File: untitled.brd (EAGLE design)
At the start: 54.8 x 54.7 mm, 25 parts

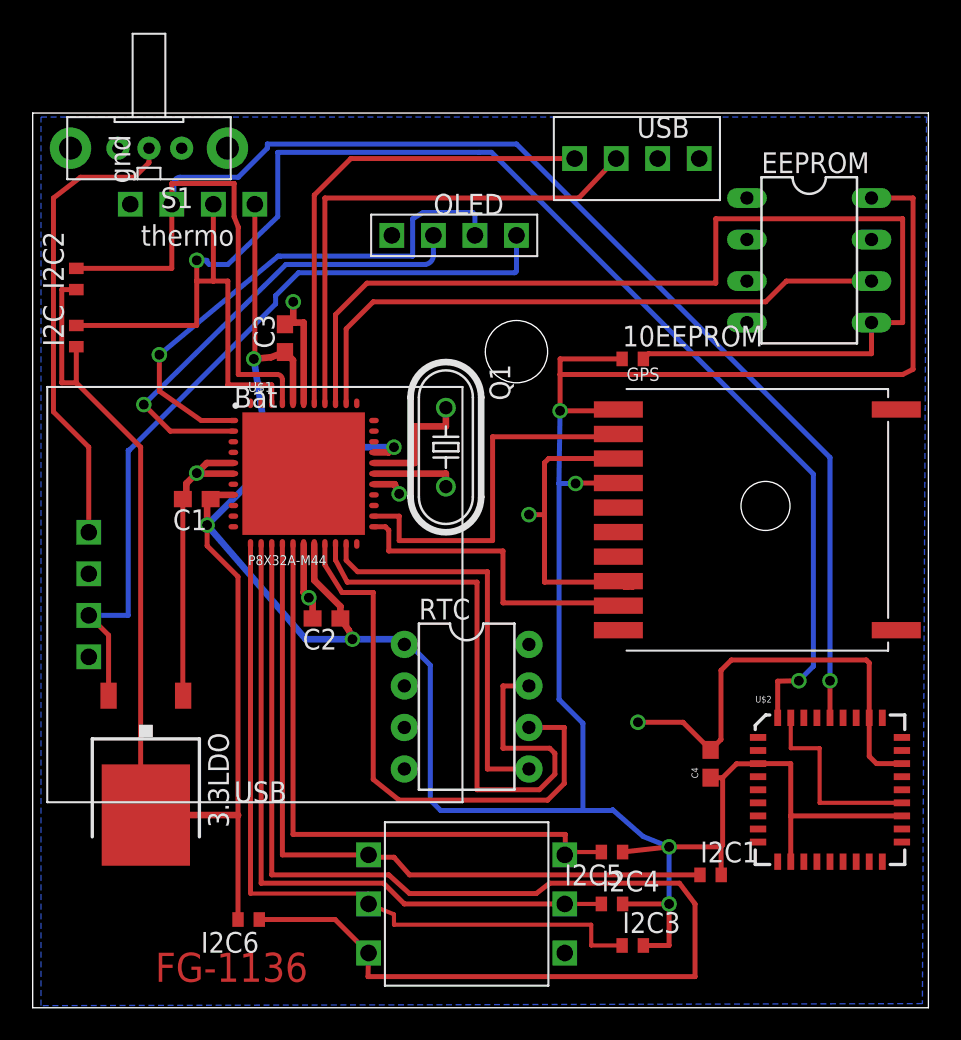
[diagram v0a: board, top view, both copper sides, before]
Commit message: fixed stupid and costly mistake with screen position
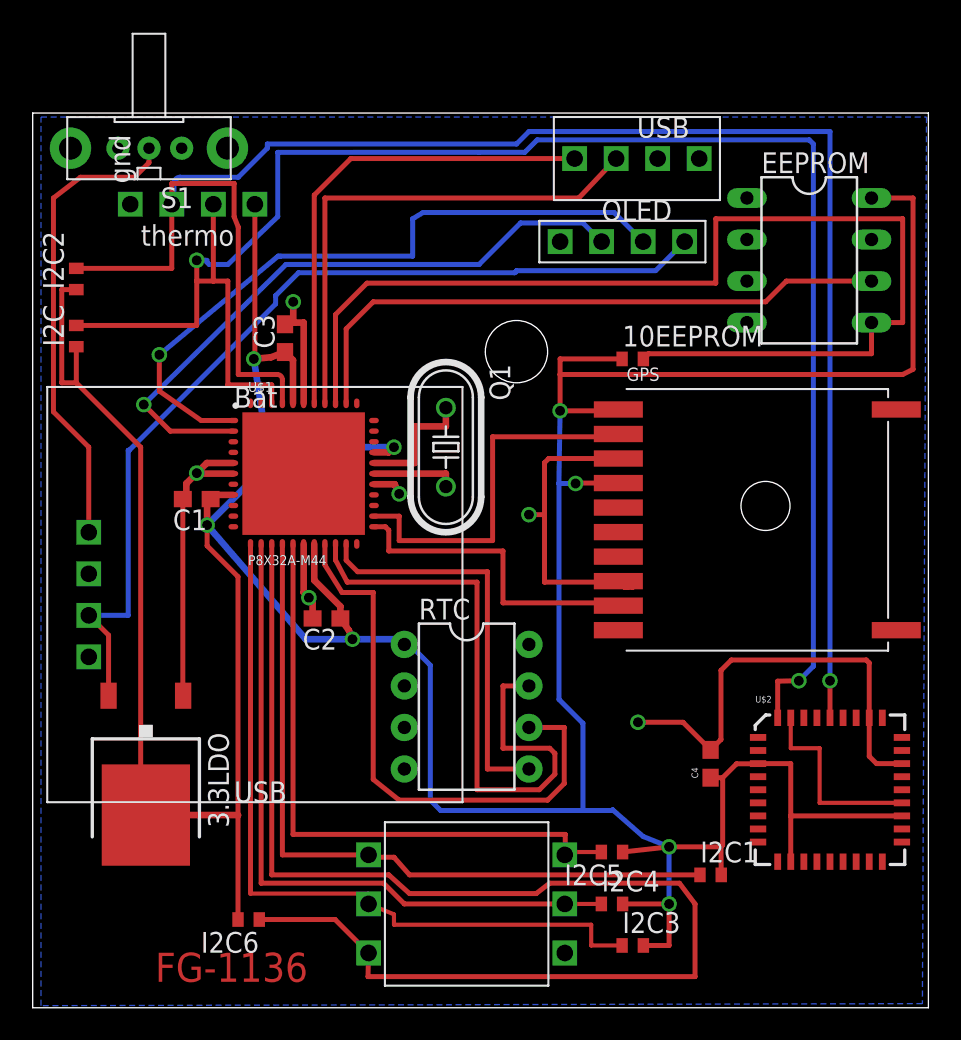
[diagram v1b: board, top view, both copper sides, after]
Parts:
- moved OLED_SCREEN 10.3 mm to (75.6, 57.0)
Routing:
- net SDA: track 95.9 -> 108.3 mm
- net SCL: track 97.3 -> 109.6 mm
- net N$10: track 28.8 -> 39.2 mm
- net N$11: track 32.5 -> 42.2 mm
- net +5V: track 48.7 -> 57.5 mm
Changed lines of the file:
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@@
 <setting verticaltext="up"/>
 </settings>
-<grid distance="0.005" unitdist="inch" unit="inch" style="lines" multiple="1" display="yes" altdistance="0.025" altunitdist="inch" altunit="inch"/>
+<grid distance="0.005" unitdist="inch" unit="inch" style="lines" multiple="1" display="no" altdistance="0.025" altunitdist="inch" altunit="inch"/>
 <layers>
 <layer number="1" name="Top" color="4" fill="1" visible="yes" active="yes"/>
@@
 <element name="GPS" library="adafruit" package="FGPMMOPA6B" value="" x="82.55" y="40.005"/>
 <element name="LIPOCHARGER-BOOSTER" library="SFLipoPack" package="SFLIPO" value="SFLIPO" x="46.736" y="36.703"/>
-<element name="OLED_SCREEN" library="4dScreen" package="4DSCREEN" value="4DSCREEN" x="65.278" y="57.404" rot="R270"/>
+<element name="OLED_SCREEN" library="4dScreen" package="4DSCREEN" value="4DSCREEN" x="75.565" y="57.023" rot="R270"/>
 <element name="RTC" library="adafruit" package="DIL08-ROUND" value="DS1302" x="64.77" y="28.575" rot="R270"/>
 <element name="S1" library="adafruit" package="EG1213" value="EG1213" x="45.339" y="62.738" rot="R180"/>
@@
 <wire x1="50.546" y1="60.579" x2="46.736" y2="60.579" width="0.3048" layer="1"/>
 <wire x1="46.736" y1="60.579" x2="46.736" y2="59.309" width="0.3048" layer="1"/>
-<wire x1="86.995" y1="43.815" x2="67.818" y2="62.992" width="0.3048" layer="16"/>
 <wire x1="67.818" y1="62.992" x2="52.578" y2="62.992" width="0.3048" layer="16"/>
 <wire x1="52.578" y1="62.992" x2="52.578" y2="62.738" width="0.3048" layer="16"/>
@@
 <wire x1="40.894" y1="55.387" x2="46.736" y2="55.387" width="0.3048" layer="1"/>
 <wire x1="46.736" y1="55.387" x2="46.736" y2="59.309" width="0.3048" layer="1"/>
-<wire x1="86.995" y1="43.815" x2="86.995" y2="30.1625" width="0.3048" layer="16"/>
 <wire x1="50.546" y1="60.579" x2="50.546" y2="58.547" width="0.3048" layer="1"/>
 <wire x1="50.546" y1="58.547" x2="50.8" y2="57.912" width="0.3048" layer="1"/>
+<wire x1="86.995" y1="30.1625" x2="86.995" y2="63.754" width="0.3048" layer="16"/>
+<wire x1="86.995" y1="63.754" x2="68.58" y2="63.754" width="0.3048" layer="16"/>
+<wire x1="68.58" y1="63.754" x2="67.818" y2="62.992" width="0.3048" layer="16"/>
 </signal>
 <signal name="SDA">
@@
 <wire x1="48.26" y1="55.88" x2="48.768" y2="55.88" width="0.3048" layer="16"/>
 <wire x1="48.768" y1="55.88" x2="48.895" y2="55.88" width="0.3048" layer="16"/>
-<wire x1="65.532" y1="62.484" x2="66.294" y2="62.484" width="0.3048" layer="16"/>
-<wire x1="66.294" y1="62.484" x2="85.979" y2="42.799" width="0.3048" layer="16"/>
 <wire x1="53.21680625" y1="62.4820625" x2="53.21680625" y2="58.55080625" width="0.3048" layer="16"/>
 <wire x1="53.21680625" y1="58.55080625" x2="50.165" y2="55.626" width="0.3048" layer="16"/>
@@
 <wire x1="48.26" y1="51.8945" x2="48.26" y2="54.61" width="0.3048" layer="1"/>
 <wire x1="85.09" y1="30.1625" x2="85.979" y2="31.0515" width="0.3048" layer="16"/>
-<wire x1="85.979" y1="31.0515" x2="85.979" y2="42.799" width="0.3048" layer="16"/>
+<wire x1="85.979" y1="31.0515" x2="85.979" y2="62.992" width="0.3048" layer="16"/>
+<wire x1="85.979" y1="62.992" x2="85.725" y2="63.246" width="0.3048" layer="16"/>
+<wire x1="85.725" y1="63.246" x2="69.088" y2="63.246" width="0.3048" layer="16"/>
+<wire x1="65.532" y1="62.484" x2="68.326" y2="62.484" width="0.3048" layer="16"/>
+<wire x1="68.326" y1="62.484" x2="69.088" y2="63.246" width="0.3048" layer="16"/>
 </signal>
 <signal name="N$3">
@@
 <wire x1="46.6437" y1="45.4313" x2="45.0215" y2="47.0535" width="0.3048" layer="1"/>
 <wire x1="45.0215" y1="47.0535" x2="53.721" y2="55.626" width="0.3048" layer="16"/>
-<wire x1="53.721" y1="55.626" x2="62.23" y2="55.626" width="0.3048" layer="16"/>
-<wire x1="62.23" y1="55.626" x2="62.738" y2="56.261" width="0.3048" layer="16" curve="90"/>
-<wire x1="62.738" y1="56.261" x2="62.738" y2="57.404" width="0.3048" layer="16"/>
+<wire x1="53.721" y1="55.626" x2="65.532" y2="55.626" width="0.3048" layer="16"/>
+<wire x1="73.025" y1="57.023" x2="71.882" y2="58.166" width="0.3048" layer="16"/>
+<wire x1="71.882" y1="58.166" x2="68.072" y2="58.166" width="0.3048" layer="16"/>
+<wire x1="68.072" y1="58.166" x2="65.532" y2="55.626" width="0.3048" layer="16"/>
 </signal>
 <signal name="N$11">
@@
 <wire x1="48.5337" y1="46.0813" x2="45.974" y2="47.879" width="0.3048" layer="1"/>
 <wire x1="45.974" y1="47.879" x2="45.974" y2="50.1015" width="0.3048" layer="1"/>
-<wire x1="65.278" y1="57.404" x2="65.278" y2="58.674" width="0.3048" layer="16"/>
-<wire x1="65.278" y1="58.674" x2="65.151" y2="58.801" width="0.3048" layer="16"/>
-<wire x1="65.151" y1="58.801" x2="62.103" y2="58.801" width="0.3048" layer="16"/>
 <wire x1="62.103" y1="58.801" x2="61.468" y2="58.42" width="0.3048" layer="16"/>
 <wire x1="61.468" y1="58.42" x2="61.468" y2="56.134" width="0.3048" layer="16"/>
 <wire x1="61.468" y1="56.134" x2="53.3793125" y2="56.134" width="0.3048" layer="16"/>
 <wire x1="53.3793125" y1="56.134" x2="53.24675" y2="56.1395625" width="0.3048" layer="16"/>
+<wire x1="75.565" y1="57.023" x2="73.787" y2="58.801" width="0.3048" layer="16"/>
+<wire x1="73.787" y1="58.801" x2="62.103" y2="58.801" width="0.3048" layer="16"/>
 </signal>
 <signal name="N$18">
@@
 <contactref element="OLED_SCREEN" pad="5V"/>
 <contactref element="3.3LDO" pad="2"/>
-<wire x1="67.818" y1="57.404" x2="67.818" y2="55.245" width="0.3048" layer="16"/>
 <wire x1="67.818" y1="55.245" x2="67.691" y2="55.118" width="0.3048" layer="16" curve="-90"/>
 <wire x1="67.691" y1="55.118" x2="54.483" y2="55.118" width="0.3048" layer="16"/>
@@
 <wire x1="44.069" y1="44.2595" x2="44.069" y2="34.163" width="0.3048" layer="16"/>
 <wire x1="44.069" y1="34.163" x2="41.656" y2="34.163" width="0.3048" layer="16"/>
+<wire x1="78.105" y1="57.023" x2="76.327" y2="55.245" width="0.3048" layer="16"/>
+<wire x1="76.327" y1="55.245" x2="67.818" y2="55.245" width="0.3048" layer="16"/>
 </signal>
 <signal name="+3V3">
